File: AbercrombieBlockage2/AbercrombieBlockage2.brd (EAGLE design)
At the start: 38 x 38 mm, 35 parts, among them U1 DMN3135LVT, U2 ICS-43434, U3 CYBLE-022001-00, U4 LIS3DH, U5 VL53L0X, U6 VL53L0X, U7 VL53L0X, U8 M24

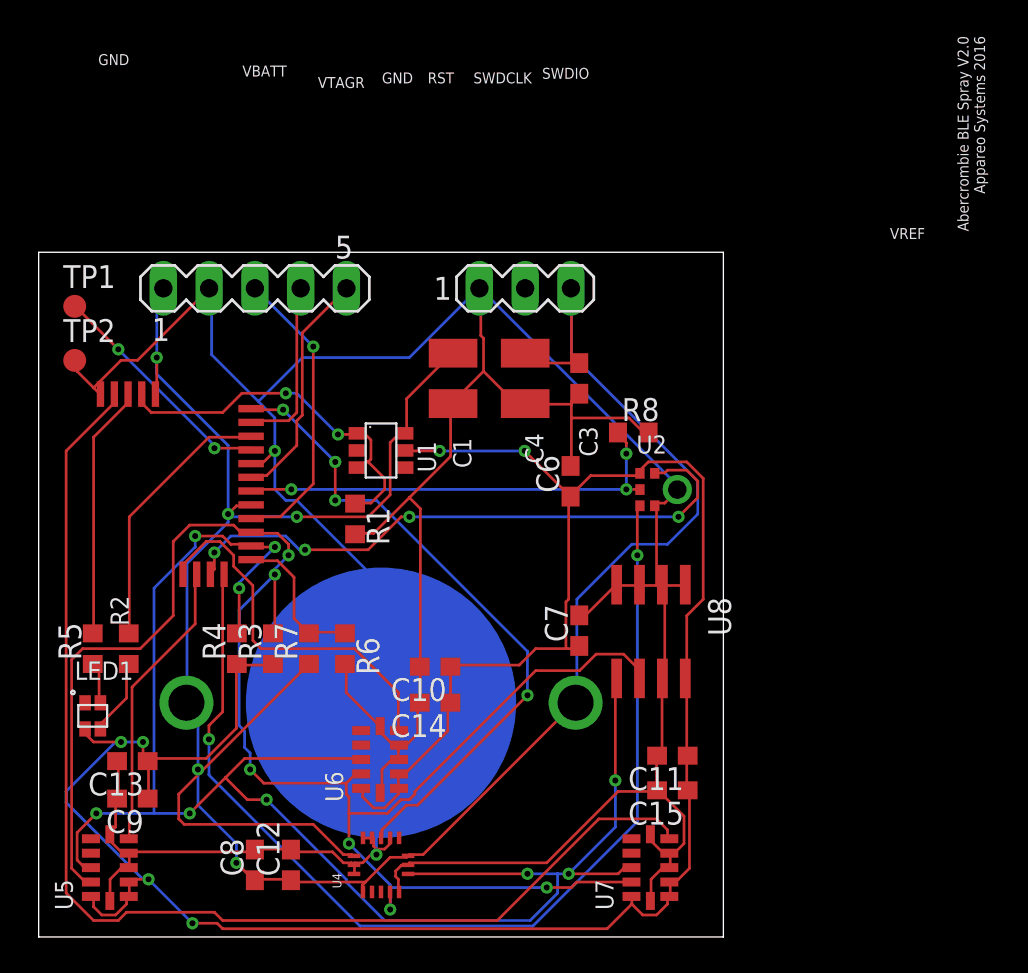
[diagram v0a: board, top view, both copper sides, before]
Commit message: Autorouted the AbercrombieLaser spray monitor
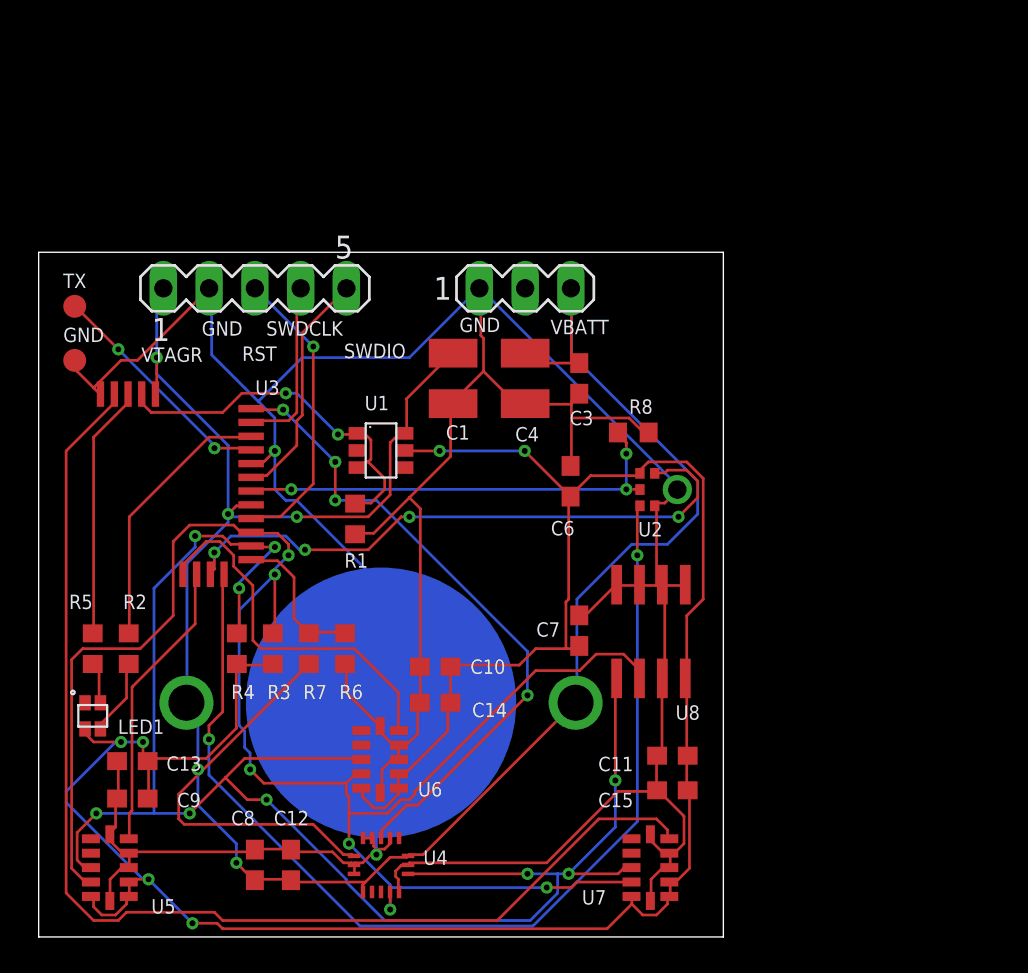
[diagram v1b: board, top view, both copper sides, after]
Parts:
- renumbered TP1 to TX, TP2 to GND
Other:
- board text added: "Abercrombie BLE LaserSpray V1.0 Appareo Systems 2016"
- board text removed: "Abercrombie BLE Spray V2.0 Appareo Systems 2016"
- board text removed: "VREF"

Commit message: Routed the Abercrombie Laser project.
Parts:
- moved R8 33.4 mm to (4.25, 11.0), turned to 180 degrees
- moved LED1 32.2 mm to (35.0, 15.7), turned to 180 degrees
- moved U2 29.7 mm to (5.63, 14.2), turned to 180 degrees
- moved R5 29.0 mm to (32.0, 15.0), turned to 180 degrees
- moved R2 27.0 mm to (32.0, 17.0), turned to 180 degrees
- moved C6 21.7 mm to (11.0, 14.0)
- moved GND 15.9 mm to (17.4, 27.9)
- moved SV2 15.6 mm to (25.1, 27.5)
- moved TX 15.3 mm to (15.6, 27.9)
- moved C7 15.2 mm to (24.0, 3.00), turned to 180 degrees
- moved SV1 13.0 mm to (34.0, 25.0), turned to 90 degrees
- moved U1 12.5 mm to (25.0, 16.0)
- moved U8 12.0 mm to (25.0, 8.95)
- moved C1 8.06 mm to (24.0, 23.0)
- moved C3 8.06 mm to (31.0, 23.0)
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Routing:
- net GND: track 214.3 -> 13.1 mm, vias 2 -> 18
- net WS: track 58.8 -> 8.69 mm, vias 2 -> 0
- net VDD: track 142.5 -> 95.0 mm, vias 5 -> 0
- net SWDCLK: track 9.75 -> 33.5 mm, vias 0 -> 2
- net SWDIO: track 13.1 -> 32.7 mm, vias 0 -> 1
- net SCK: track 33.6 -> 15.5 mm, vias 4 -> 0
- net GREEN_LED: track 14.1 -> 30.8 mm, vias 0 -> 4
- net XSHUT_3: track 66.3 -> 50.5 mm, vias 0 -> 4
- net V+: track 138.3 -> 122.8 mm, vias 6 -> 9
- net XRES: track 16.4 -> 30.2 mm, vias 1 -> 0
- net XSHUT_2: track 20.7 -> 34.3 mm, vias 0 -> 2
- net SCL: track 98.2 -> 85.2 mm, vias 6 -> 5
- net WAKEUP: track 36.2 -> 23.4 mm, vias 4 -> 2
- net SDI: track 25.0 -> 12.8 mm, vias 3 -> 0
- net BLUE_LED: track 15.1 -> 27.0 mm, vias 0 -> 4
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- added copper zone on layer 1, net GND
- added copper zone on layer 16, net GND
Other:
- board size 38 x 38 mm -> 38 x 30 mm
